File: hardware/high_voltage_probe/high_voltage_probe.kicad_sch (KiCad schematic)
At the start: 18 parts, among them J1 SMA

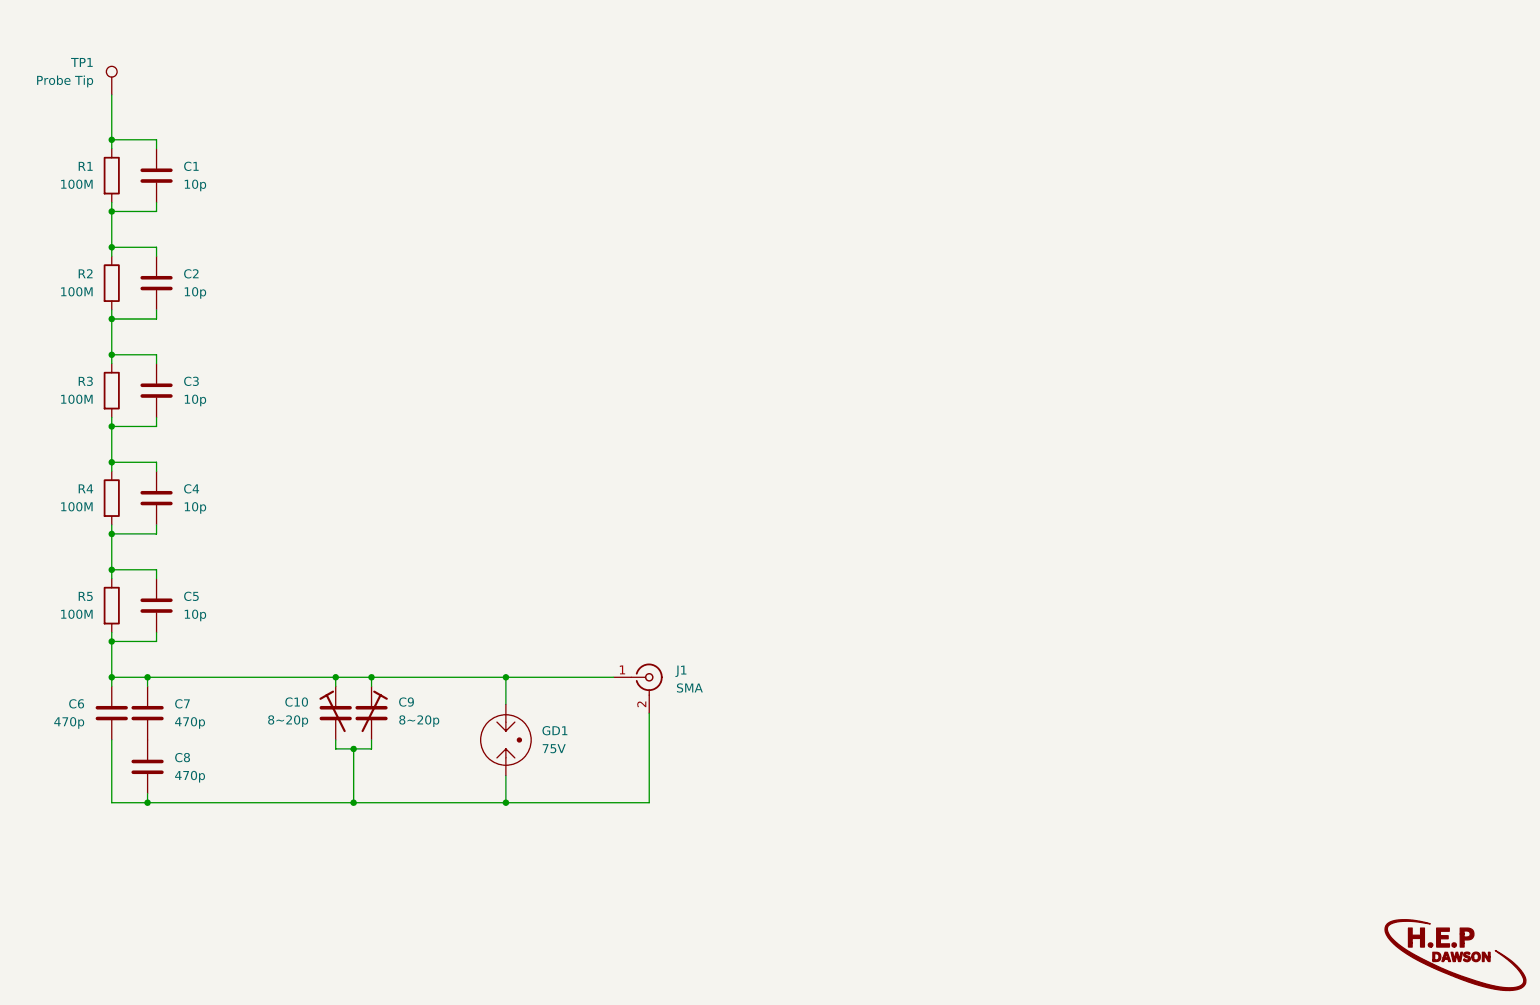
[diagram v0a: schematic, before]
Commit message: update hv probe schematic
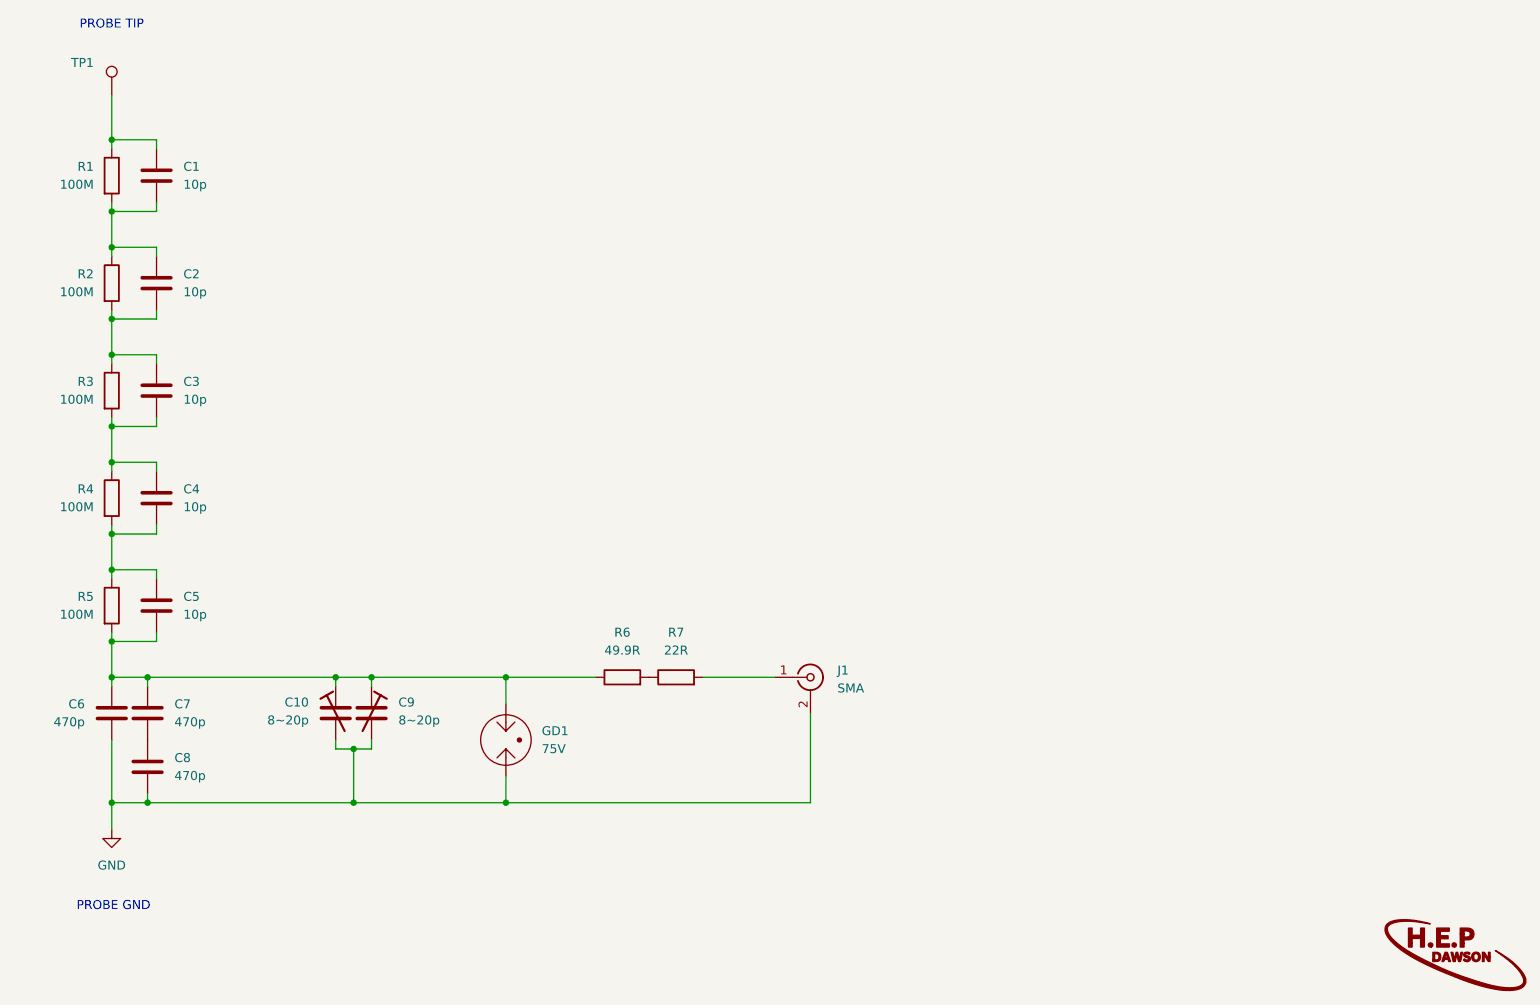
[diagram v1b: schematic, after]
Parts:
- added R6: 49.9R, symbol Device:R
- added R7: 22R, symbol Device:R
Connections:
- net at C10.1, C5.2, C6.1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: now also R6.1; no longer J1.1 (In)
- net GND: now reaches C10.2, C6.2, C8.2, C9.2, GD1.1, J1.2 (Ext)
- new net: R6.2, R7.1
- new net: J1.1 (In), R7.2
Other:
- note added: "PROBE GND"
- note added: "PROBE TIP"
- moved on the sheet: J1
